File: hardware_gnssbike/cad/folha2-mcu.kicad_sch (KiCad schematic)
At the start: 14 parts, among them J201 Tag-Connect TC2030-NL, U201 MinewSemi ME54BS13

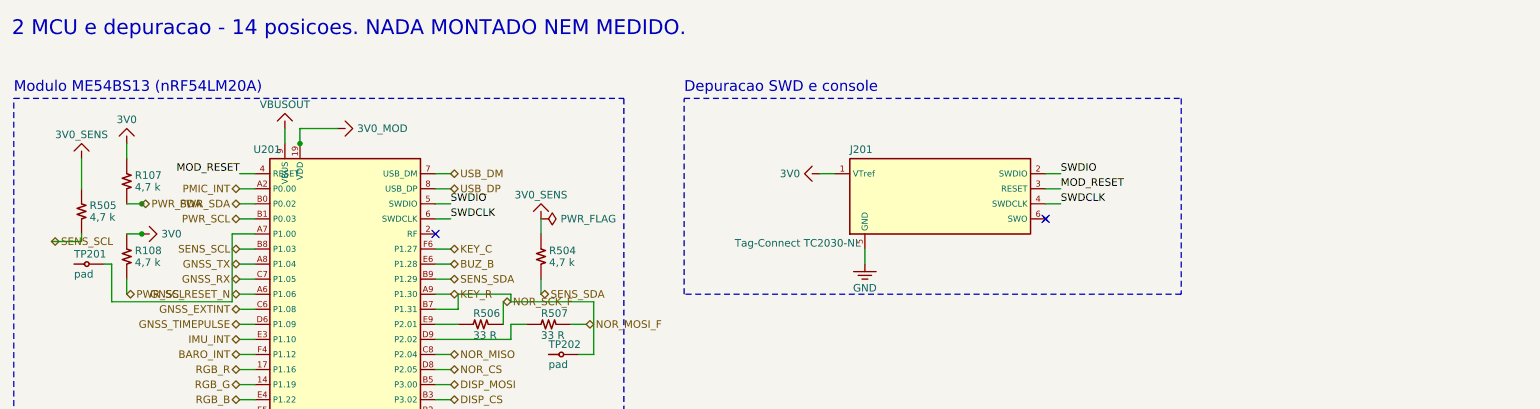
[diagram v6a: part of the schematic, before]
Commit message: feat(hardware): the 10-way SWD header, and a case proposal around the board
Two of the owner's requests of 2026-09-26.

J202: the ARM Cortex Debug Connector, 2 x 5 at 1,27 mm, SMD and without
its shroud (2,5 mm: the shrouded part, 4,83 mm, does not fit under the
lid), beside the Tag-Connect pads and on the same nets, where the J-Link's
9-pin Cortex-M adapter plugs in without a clip. SWDCLK and nRESET are
passive on it so that the ERC does not see two outputs on one net. Left as
a JUNTO of the module the placer put it under the display; it is placed
explicitly at (11,3; 72,2), below the keys, right of the M2 hole's square
and left of the USB pair's corridor. Schematic re-verified against the
netlist; the board re-placed, re-routed and re-checked (24 rules met, 5
failed as before: RF9, AL1, AL2, ME2, RT1 with 46 unconnected in 31 nets).

The case: 62 x 104 x 17 mm around today's 34 x 90 board, drawn by
make_caixa.py from the board file and its GLB. Cell glued on the floor
between four ribs, board on one M2 boss and three posts (its other hole is
over the cell), display glued under the lid round the window, three square
key caps spread across the display at the concept's 14 mm pitch with a bar
under the lid to each switch (the module's antenna keep-out stops the
third switch at x 21,5 on the board), a TPU membrane in a recess over
them, two solar modules on a flat facet below the keys and two on each
45-degree bevel, all in pockets under clear covers with wire holes, USB-C
notch in the bottom wall and lid rim, buzzer and barometer holes in the
floor, LED and light-sensor windows at proposed positions because both
parts are under the display today, four M2 corner screws. Out: a 3-page
PDF (front, inside, sections A-A and B-B, key and pocket details, premises,
what does not fit, parts), three 3D views and eight STL files for a first
print. Nothing printed, nothing measured on hardware; the USB door, the
external-antenna bracket and the whole-case dry run are the next rou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
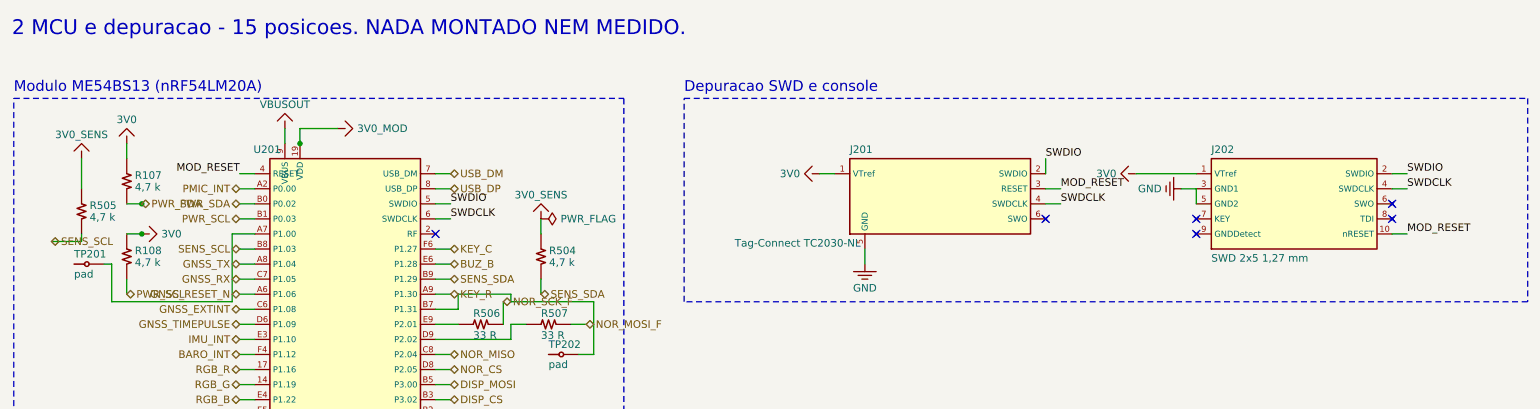
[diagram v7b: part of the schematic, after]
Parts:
- added J202: SWD 2x5 1,27 mm, Connector_PinHeader_1.27mm:PinHeader_2x05_P1.27mm_Vertical_SMD, symbol gnssbike:J202
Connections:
- net 3V0: now also J202.1 (VTref)
- net GND: now also J202.3 (GND1), J202.5 (GND2)
- net MOD_RESET: now also J202.10 (nRESET)
- net SWDCLK: now also J202.4 (SWDCLK)
- net SWDIO: now also J202.2 (SWDIO)
- no-connect marks 2 -> 6
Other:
- note added: "2 MCU e depuracao - 15 posicoes. NADA MONTADO NEM MEDIDO."
- note removed: "2 MCU e depuracao - 14 posicoes. NADA MONTADO NEM MEDIDO."
